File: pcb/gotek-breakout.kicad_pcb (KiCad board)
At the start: 2 copper layers, 101.6 x 76.5 mm, 15 parts, among them J1 FFC 10x1 0.5mm, J10 FFC 10x1 0.5mm, J11 USB Breakout, J2 USB_A, J3 OLED, J4 Encoder, J7 J7 Right Angle Connector, J8 J8 Mirror

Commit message: Revision 2
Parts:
- added D11: LED, LED_THT:LED_D3.0mm, F.Cu at (73.8, 49.7)
- added H7: MountingHole_3.2mm_M3, MountingHole:MountingHole_3.2mm_M3, F.Cu at (90.5, 101.0)
- added J12: Activity LED Cathode, Connector_PinHeader_2.54mm:PinHeader_1x01_P2.54mm_Vertical, F.Cu at (83.7, 100.0)
- added R11: 10K, Resistor_THT:R_Axial_DIN0411_L9.9mm_D3.6mm_P12.70mm_Horizontal, B.Cu at (82.3, 42.3)
- C1: moved to B.Cu
- moved J3 32.9 mm to (78.0, 53.6), turned to 180 degrees
- moved H6 22.4 mm to (84.5, 129.9)
- moved J4 22.2 mm to (117.5, 44.9), turned to 0 degrees
- moved J10 17.6 mm to (90.4, 122.0), turned to 90 degrees
- moved C1 13.2 mm to (56.4, 55.5), turned to -90 degrees
- moved J1 12.8 mm to (95.0, 57.1), turned to 180 degrees
- moved J11 1.44 mm to (78.5, 100.0)
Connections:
- J1 pad 3: /+3V -> /ACT_LED_SINK
- J10 pad 8: /Gotek Side/+3V -> /Gotek Side/ACT_LED_SINK
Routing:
- net /Gotek Side/+3V: track 35.2 -> 0.00 mm, vias 1 -> 0
- net /ACT_LED_SINK: track 0.00 -> 30.9 mm, vias 0 -> 1
- net /Gotek Side/ACT_LED_SINK: track 0.00 -> 23.6 mm
- net /Gotek Side/ROT_SW: track 16.0 -> 38.1 mm
- net /Gotek Side/ROT_DT: track 15.0 -> 36.8 mm
- net /Gotek Side/+5V: track 19.3 -> 40.0 mm, vias 1 -> 0
- net /Gotek Side/ROT_CLK: track 13.4 -> 34.1 mm
- net /Gotek Side/OLED_SDA: track 30.6 -> 49.8 mm, vias 0 -> 1
- net /ROT_DT: track 46.2 -> 28.5 mm
- net /ROT_CLK: track 46.1 -> 29.0 mm
- net /ROT_SW: track 46.3 -> 29.7 mm
- net /Gotek Side/OLED_SCK: track 37.1 -> 53.2 mm, vias 0 -> 1
- net /Gotek Side/USB_D-: track 10.5 -> 26.3 mm
- net /Gotek Side/USB_D+: track 14.1 -> 26.3 mm
- net Net-(D11-A): track 0.00 -> 8.06 mm
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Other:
- board size 101.6 x 76.5 mm -> 101.5 x 93 mm
- board text added: "ACT"
- board text added: "J7 CONNECTS VIA RIGHT ANGLE 2X2 J8 JUMPER OR DUPONT J11 SOLDER TO RIGHT SIDE OF R1,R2 J12 [OPT] REPLACES - LEG OF L4 LED"
- board text added: "L4-"
- board text removed: "J7 CONNECTS VIA RIGHT-ANGLE 2X2 J8 JUMPER WIRE OR DUPONT J11 SOLDER TO RIGHT SIDE OF R1,R2"

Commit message: Move FFC up
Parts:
- moved J1 2.23 mm to (95.0, 54.9)
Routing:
- net /USB_D+: track 39.7 -> 41.7 mm
- net /USB_D-: track 37.6 -> 39.7 mm
- net /ROT_SW: track 29.7 -> 27.7 mm
- net /OLED_SDA: track 21.9 -> 20.7 mm, vias 1 -> 0
- net /+5V: track 89.3 -> 88.1 mm
- net /ROT_CLK: track 29.0 -> 27.9 mm
- net /GND: track 4.45 -> 3.43 mm, vias 15 -> 14
- net /ROT_DT: track 28.5 -> 27.8 mm
- net /OLED_SCK: track 21.1 -> 20.6 mm, vias 1 -> 0

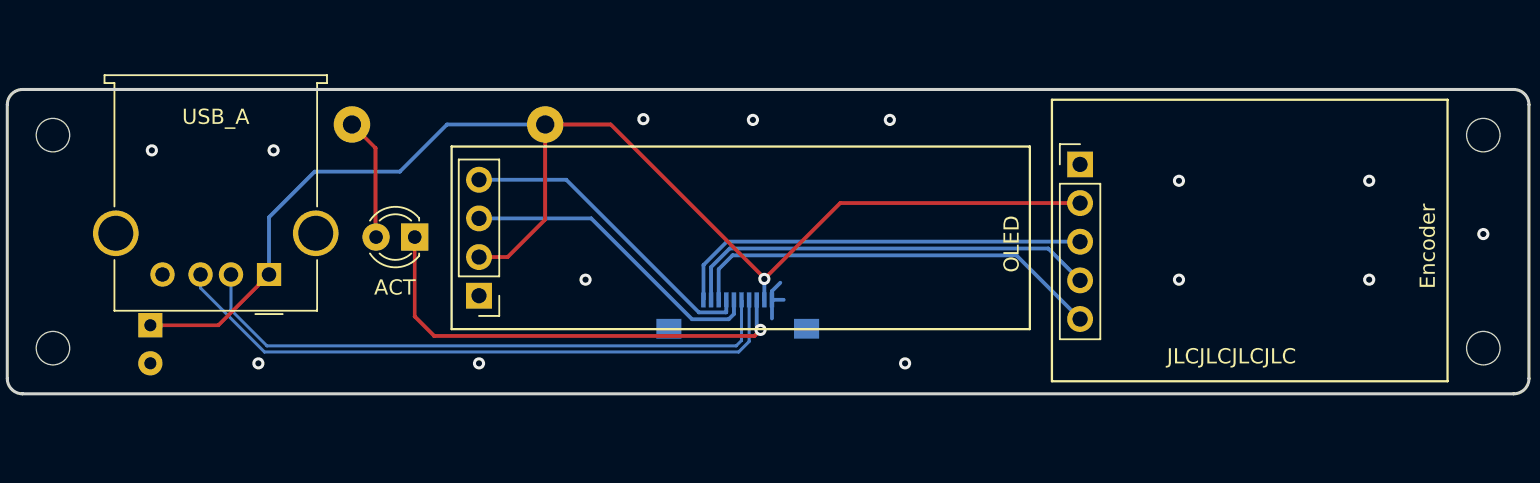
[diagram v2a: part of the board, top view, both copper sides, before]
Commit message: Nudging items on PCB for rev3
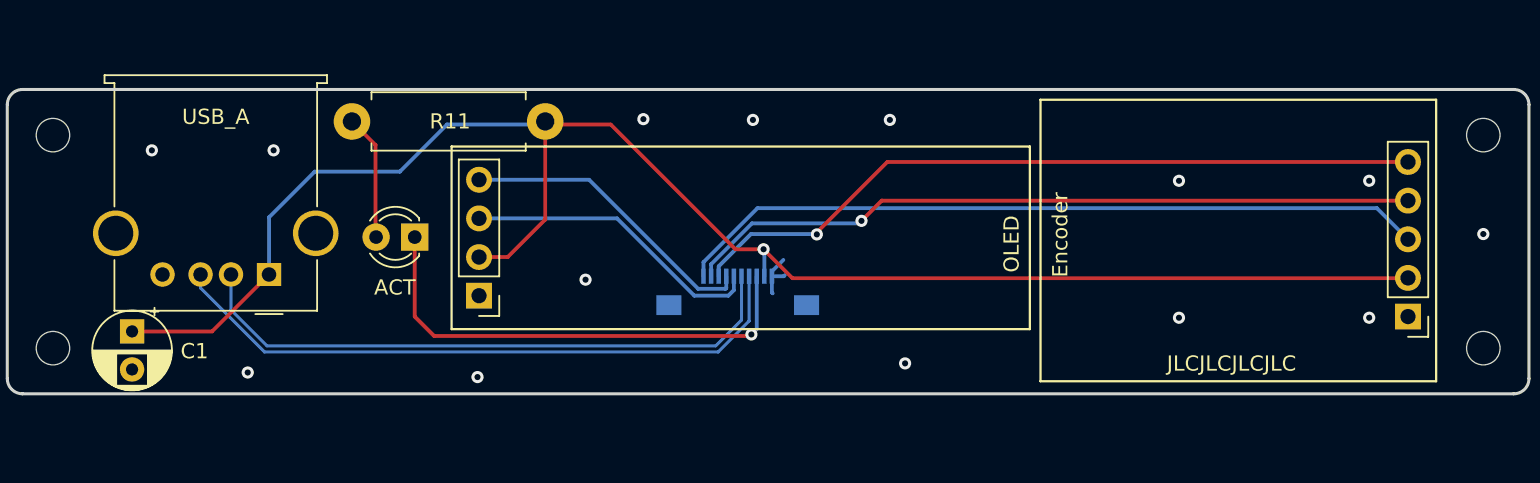
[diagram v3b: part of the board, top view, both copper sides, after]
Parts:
- C1, R11: moved to F.Cu
- moved J4 23.8 mm to (139.1, 54.9), turned to 180 degrees
- moved J1 1.55 mm to (95.0, 53.3)
- moved C1 1.27 mm to (55.2, 55.9)
- moved R11 0.20 mm to (82.3, 42.1)
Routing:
- net /ROT_SW: track 27.7 -> 49.5 mm
- net /+5V: track 88.1 -> 109.7 mm
- net /ROT_CLK: track 27.9 -> 48.9 mm, vias 0 -> 1
- net /ROT_DT: track 27.8 -> 48.3 mm, vias 0 -> 1
- net /ACT_LED_SINK: track 30.7 -> 31.9 mm
- net /USB_D+: track 41.7 -> 42.5 mm
- net /USB_D-: track 39.7 -> 40.4 mm
- net /OLED_SCK: track 20.6 -> 19.9 mm
- net /OLED_SDA: track 20.7 -> 20.0 mm
